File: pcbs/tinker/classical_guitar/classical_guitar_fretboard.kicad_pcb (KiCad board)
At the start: 2 copper layers, 192 parts, among them Q1 AO3401A, U1 AT42QT1110-A, U2 AT42QT1110-A, U3 AT42QT1110-A, U4 MP2359

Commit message: Layed out AT32QT1110
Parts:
- moved JPmiso3 419.5 mm to (77.8, 172.2)
- moved JPsck3 419.5 mm to (72.2, 172.2)
- moved Rs26 407.5 mm to (60.1, 173.8), turned to 90 degrees
- moved Cs25 405.5 mm to (55.4, 171.2), turned to 180 degrees
- moved Cs21 403.5 mm to (53.2, 157.5)
- moved Cd5 398.5 mm to (52.2, 164.0), turned to 270 degrees
- moved Cd6 398.4 mm to (59.9, 164.1), turned to 90 degrees
- moved Rs36 397.7 mm to (57.7, 156.6), turned to 90 degrees
- moved Cs23 397.7 mm to (50.8, 166.9), turned to 270 degrees
- moved Rs39 392.6 mm to (55.9, 156.6), turned to 270 degrees
- moved Cs26 388.6 mm to (59.1, 171.2), turned to 180 degrees
- moved Rs25 383.4 mm to (56.3, 173.8), turned to 90 degrees
- moved Rs28 381.5 mm to (67.6, 162.7)
- moved Cs30 380.6 mm to (60.5, 157.5)
- moved JPmosi3 376.1 mm to (64.4, 172.7), turned to 90 degrees
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- renumbered Cs11 to Cs1, Cs20 to Cs10, Cs21 to Cs11, Cs22 to Cs12, Cs23 to Cs13, Cs24 to Cs14, Cs25 to Cs15, Cs26 to Cs16, Cs27 to Cs17, Cs28 to Cs18, Cs29 to Cs19, Cs12 to Cs2, Cs30 to Cs20, Cs1 to Cs21, Cs2 to Cs22, Cs3 to Cs23, Cs4 to Cs24, Cs5 to Cs25, Cs6 to Cs26, Cs7 to Cs27, Cs8 to Cs28, Cs9 to Cs29, Cs13 to Cs3, Cs10 to Cs30, Cs14 to Cs4, Cs15 to Cs5, Cs16 to Cs6, Cs17 to Cs7, Cs18 to Cs8, Cs19 to Cs9
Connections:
- Cs1 pad 1: Net-(Cs11-Pad1) -> Net-(Cs1-Pad1)
- Cs10 pad 1: Net-(Cs20-Pad1) -> Net-(Cs10-Pad1)
- Cs11 pad 1: Net-(Cs21-Pad1) -> Net-(Cs11-Pad1)
- Cs12 pad 1: Net-(Cs22-Pad1) -> Net-(Cs12-Pad1)
- Cs13 pad 1: Net-(Cs23-Pad1) -> Net-(Cs13-Pad1)
- Cs14 pad 1: Net-(Cs24-Pad1) -> Net-(Cs14-Pad1)
- Cs15 pad 1: Net-(Cs25-Pad1) -> Net-(Cs15-Pad1)
- Cs16 pad 1: Net-(Cs26-Pad1) -> Net-(Cs16-Pad1)
- Cs17 pad 1: Net-(Cs27-Pad1) -> Net-(Cs17-Pad1)
- Cs18 pad 1: Net-(Cs28-Pad1) -> Net-(Cs18-Pad1)
- Cs19 pad 1: Net-(Cs29-Pad1) -> Net-(Cs19-Pad1)
- Cs2 pad 1: Net-(Cs12-Pad1) -> Net-(Cs2-Pad1)
- Cs20 pad 1: Net-(Cs30-Pad1) -> Net-(Cs20-Pad1)
- Cs21 pad 1: Net-(Cs1-Pad1) -> Net-(Cs21-Pad1)
- Cs22 pad 1: Net-(Cs2-Pad1) -> Net-(Cs22-Pad1)
- Cs23 pad 1: Net-(Cs3-Pad1) -> Net-(Cs23-Pad1)
- Cs24 pad 1: Net-(Cs4-Pad1) -> Net-(Cs24-Pad1)
- Cs25 pad 1: Net-(Cs5-Pad1) -> Net-(Cs25-Pad1)
- Cs26 pad 1: Net-(Cs6-Pad1) -> Net-(Cs26-Pad1)
- Cs27 pad 1: Net-(Cs7-Pad1) -> Net-(Cs27-Pad1)
- Cs28 pad 1: Net-(Cs8-Pad1) -> Net-(Cs28-Pad1)
- Cs29 pad 1: Net-(Cs9-Pad1) -> Net-(Cs29-Pad1)
- Cs3 pad 1: Net-(Cs13-Pad1) -> Net-(Cs3-Pad1)
- Cs30 pad 1: Net-(Cs10-Pad1) -> Net-(Cs30-Pad1)
- Cs4 pad 1: Net-(Cs14-Pad1) -> Net-(Cs4-Pad1)
- Cs5 pad 1: Net-(Cs15-Pad1) -> Net-(Cs5-Pad1)
- Cs6 pad 1: Net-(Cs16-Pad1) -> Net-(Cs6-Pad1)
- Cs7 pad 1: Net-(Cs17-Pad1) -> Net-(Cs7-Pad1)
- Cs8 pad 1: Net-(Cs18-Pad1) -> Net-(Cs8-Pad1)
- Cs9 pad 1: Net-(Cs19-Pad1) -> Net-(Cs9-Pad1)
- Rs1 pad 1: /Electrode21 -> /Electrode1
- Rs10 pad 1: /Electrode30 -> /Electrode10
- Rs11 pad 1: /Electrode1 -> /Electrode11
- Rs12 pad 1: /Electrode2 -> /Electrode12
- Rs13 pad 1: /Electrode3 -> /Electrode13
- Rs14 pad 1: /Electrode4 -> /Electrode14
- Rs15 pad 1: /Electrode5 -> /Electrode15
- Rs16 pad 1: /Electrode6 -> /Electrode16
- Rs17 pad 1: /Electrode7 -> /Electrode17
- Rs18 pad 1: /Electrode8 -> /Electrode18
- Rs19 pad 1: /Electrode9 -> /Electrode19
- Rs2 pad 1: /Electrode22 -> /Electrode2
- Rs20 pad 1: /Electrode10 -> /Electrode20
- Rs21 pad 1: /Electrode11 -> /Electrode21
- Rs22 pad 1: /Electrode12 -> /Electrode22
- Rs23 pad 1: /Electrode13 -> /Electrode23
- Rs24 pad 1: /Electrode14 -> /Electrode24
- Rs25 pad 1: /Electrode15 -> /Electrode25
- Rs26 pad 1: /Electrode16 -> /Electrode26
- Rs27 pad 1: /Electrode17 -> /Electrode27
- Rs28 pad 1: /Electrode18 -> /Electrode28
- Rs29 pad 1: /Electrode19 -> /Electrode29
- Rs3 pad 1: /Electrode23 -> /Electrode3
- Rs30 pad 1: /Electrode20 -> /Electrode30
- Rs4 pad 1: /Electrode24 -> /Electrode4
- Rs5 pad 1: /Electrode25 -> /Electrode5
- Rs6 pad 1: /Electrode26 -> /Electrode6
- Rs7 pad 1: /Electrode27 -> /Electrode7
- Rs8 pad 1: /Electrode28 -> /Electrode8
- Rs9 pad 1: /Electrode29 -> /Electrode9
- U1 pad 1: Net-(Cs11-Pad1) -> Net-(Cs1-Pad1)
- U1 pad 11: Net-(Cs15-Pad1) -> Net-(Cs5-Pad1)
- U1 pad 13: Net-(Cs16-Pad1) -> Net-(Cs6-Pad1)
- U1 pad 19: Net-(Cs17-Pad1) -> Net-(Cs7-Pad1)
- U1 pad 22: Net-(Cs18-Pad1) -> Net-(Cs8-Pad1)
- U1 pad 25: Net-(Cs19-Pad1) -> Net-(Cs9-Pad1)
- U1 pad 27: Net-(Cs20-Pad1) -> Net-(Cs10-Pad1)
- U1 pad 3: Net-(Cs12-Pad1) -> Net-(Cs2-Pad1)
- U1 pad 6: Net-(Cs13-Pad1) -> Net-(Cs3-Pad1)
- U1 pad 9: Net-(Cs14-Pad1) -> Net-(Cs4-Pad1)
- U2 pad 1: Net-(Cs21-Pad1) -> Net-(Cs11-Pad1)
- U2 pad 11: Net-(Cs25-Pad1) -> Net-(Cs15-Pad1)
- U2 pad 13: Net-(Cs26-Pad1) -> Net-(Cs16-Pad1)
- U2 pad 19: Net-(Cs27-Pad1) -> Net-(Cs17-Pad1)
- U2 pad 22: Net-(Cs28-Pad1) -> Net-(Cs18-Pad1)
- U2 pad 25: Net-(Cs29-Pad1) -> Net-(Cs19-Pad1)
- U2 pad 27: Net-(Cs30-Pad1) -> Net-(Cs20-Pad1)
- U2 pad 3: Net-(Cs22-Pad1) -> Net-(Cs12-Pad1)
- U2 pad 6: Net-(Cs23-Pad1) -> Net-(Cs13-Pad1)
- U2 pad 9: Net-(Cs24-Pad1) -> Net-(Cs14-Pad1)
- U3 pad 1: Net-(Cs1-Pad1) -> Net-(Cs21-Pad1)
- U3 pad 11: Net-(Cs5-Pad1) -> Net-(Cs25-Pad1)
- U3 pad 13: Net-(Cs6-Pad1) -> Net-(Cs26-Pad1)
- U3 pad 19: Net-(Cs7-Pad1) -> Net-(Cs27-Pad1)
- U3 pad 22: Net-(Cs8-Pad1) -> Net-(Cs28-Pad1)
- U3 pad 25: Net-(Cs9-Pad1) -> Net-(Cs29-Pad1)
- U3 pad 27: Net-(Cs10-Pad1) -> Net-(Cs30-Pad1)
- U3 pad 3: Net-(Cs2-Pad1) -> Net-(Cs22-Pad1)
- U3 pad 6: Net-(Cs3-Pad1) -> Net-(Cs23-Pad1)
- U3 pad 9: Net-(Cs4-Pad1) -> Net-(Cs24-Pad1)

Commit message: Replaced jumper pads
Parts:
- JPch1, JPch2, JPch3, JPe1, JPe10, JPe11, JPe12, JPe13, JPe14, JPe15, JPe16, JPe17, JPe18, JPe19, JPe2, JPe20, JPe21, JPe22, JPe23, JPe24, JPe25, JPe26, JPe27, JPe28, JPe29, JPe3, JPe30, JPe4, JPe5, JPe6, JPe7, JPe8, JPe9, JPmiso1, JPmiso2, JPmiso3, JPmosi1, JPmosi2, JPmosi3, JPsck1, JPsck2, JPsck3: value Jumper_3_B12 -> SolderJumper_3_Open; footprint Jumper:SolderJumper-3_P1.3mm_Bridged12_RoundedPad1.0x1.5mm_NumberLabels -> Jumper:SolderJumper-3_P1.3mm_Open_RoundedPad1.0x1.5mm_NumberLabels
- moved JPsck1 398.9 mm to (172.1, 131.6)
- moved JPmosi2 392.2 mm to (172.1, 128.1)
- moved JPe11 384.6 mm to (143.8, 131.6)
- moved JPe29 383.7 mm to (160.8, 131.6)
- moved JPe27 382.5 mm to (166.4, 124.5)
- moved JPmiso2 382.5 mm to (172.1, 124.5)
- moved JPmiso1 379.6 mm to (166.4, 128.1)
- moved JPe4 378.0 mm to (143.8, 124.5)
- moved JPe17 376.3 mm to (149.4, 131.6)
- moved JPe13 374.5 mm to (149.4, 128.1)
- moved JPe18 373.5 mm to (166.4, 117.4)
- moved JPch3 372.9 mm to (149.4, 113.9)
- moved JPe1 372.7 mm to (143.8, 121.0)
- moved JPsck2 372.5 mm to (177.7, 128.1)
- moved JPe8 371.5 mm to (160.8, 113.9)
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
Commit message: Trace for 5-to-32 decoder before replacement with 4-to-16 decoder
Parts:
- E1, E10, E11, E12, E13, E14, E15, E16, E17, E18, E19, E2, E20, E21, E22, E23, E24, E25, E26, E27, E28, E29, E3, E30, E4, E5, E6, E7, E8, E9: moved to B.Cu
- Jdecoder_output1: value Conn_02x16_Odd_Even -> Conn_01x32; footprint Connector_PinSocket_2.54mm:PinSocket_2x16_P2.54mm_Vertical -> Connector_PinSocket_2.54mm:PinSocket_1x32_P2.54mm_Vertical
- moved E30 280.6 mm to (170.0, 35.0)
- moved E21 278.2 mm to (170.0, 170.0)
- moved E29 268.4 mm to (170.0, 50.0)
- moved E22 265.9 mm to (170.0, 155.0)
- moved E28 258.7 mm to (170.0, 65.0)
- moved E20 258.5 mm to (155.0, 35.0)
- moved E23 258.0 mm to (170.0, 140.0)
- moved E11 257.8 mm to (155.0, 170.0)
- moved E27 252.5 mm to (170.0, 80.0)
- moved E24 251.0 mm to (170.0, 125.0)
- moved E25 248.9 mm to (170.0, 110.0)
- moved E26 248.6 mm to (170.0, 95.0)
- moved E19 245.9 mm to (155.0, 50.0)
- moved E12 244.3 mm to (155.0, 155.0)
- moved E10 239.6 mm to (140.0, 35.0)
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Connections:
- net /~OSS1 renamed /5_to_32_decoder/~Y0
- net /~OSS10 renamed /5_to_32_decoder/~Y9
- net /~OSS11 renamed /5_to_32_decoder/~Y10
- net /~OSS12 renamed /5_to_32_decoder/~Y11
- net /~OSS13 renamed /5_to_32_decoder/~Y12
- net /~OSS14 renamed /5_to_32_decoder/~Y13
- net /~OSS15 renamed /5_to_32_decoder/~Y14
- net /~OSS16 renamed /5_to_32_decoder/~Y15
- net /~OSS17 renamed /5_to_32_decoder/~Y16
- net /~OSS18 renamed /5_to_32_decoder/~Y17
- net /~OSS19 renamed /5_to_32_decoder/~Y18
- net /~OSS2 renamed /5_to_32_decoder/~Y1
- net /~OSS20 renamed /5_to_32_decoder/~Y19
- net /~OSS21 renamed /5_to_32_decoder/~Y20
- net /~OSS22 renamed /5_to_32_decoder/~Y21
- net /~OSS23 renamed /5_to_32_decoder/~Y22
- net /~OSS24 renamed /5_to_32_decoder/~Y23
- net /~OSS25 renamed /5_to_32_decoder/~Y24
- net /~OSS26 renamed /5_to_32_decoder/~Y25
- net /~OSS27 renamed /5_to_32_decoder/~Y26
- net /~OSS28 renamed /5_to_32_decoder/~Y27
- net /~OSS29 renamed /5_to_32_decoder/~Y28
- net /~OSS3 renamed /5_to_32_decoder/~Y2
- net /~OSS30 renamed /5_to_32_decoder/~Y29
- net /~OSS31 renamed /5_to_32_decoder/~Y30
- net /~OSS32 renamed /5_to_32_decoder/~Y31
- net /~OSS4 renamed /5_to_32_decoder/~Y3
- net /~OSS5 renamed /5_to_32_decoder/~Y4
- net /~OSS6 renamed /5_to_32_decoder/~Y5
- net /~OSS7 renamed /5_to_32_decoder/~Y6
- net /~OSS8 renamed /5_to_32_decoder/~Y7
- net /~OSS9 renamed /5_to_32_decoder/~Y8
- JPe1 pad 1: /Electrode1 -> Net-(E1-Pad1)
- JPe1 pad 2: Net-(E1-Pad1) -> /Electrode1
- JPe10 pad 1: /Electrode10 -> Net-(E10-Pad1)
- JPe10 pad 2: Net-(E10-Pad1) -> /Electrode10
- JPe11 pad 1: /Electrode11 -> Net-(E11-Pad1)
- JPe11 pad 2: Net-(E11-Pad1) -> /Electrode11
- JPe12 pad 1: /Electrode12 -> Net-(E12-Pad1)
- JPe12 pad 2: Net-(E12-Pad1) -> /Electrode12
- JPe13 pad 1: /Electrode13 -> Net-(E13-Pad1)
- JPe13 pad 2: Net-(E13-Pad1) -> /Electrode13
- JPe14 pad 1: /Electrode14 -> Net-(E14-Pad1)
- JPe14 pad 2: Net-(E14-Pad1) -> /Electrode14
- JPe15 pad 1: /Electrode15 -> Net-(E15-Pad1)
- JPe15 pad 2: Net-(E15-Pad1) -> /Electrode15
- JPe16 pad 1: /Electrode16 -> Net-(E16-Pad1)
- JPe16 pad 2: Net-(E16-Pad1) -> /Electrode16
- JPe17 pad 1: /Electrode17 -> Net-(E17-Pad1)
- JPe17 pad 2: Net-(E17-Pad1) -> /Electrode17
- JPe18 pad 1: /Electrode18 -> Net-(E18-Pad1)
- JPe18 pad 2: Net-(E18-Pad1) -> /Electrode18
- JPe19 pad 1: /Electrode19 -> Net-(E19-Pad1)
- JPe19 pad 2: Net-(E19-Pad1) -> /Electrode19
- JPe2 pad 1: /Electrode2 -> Net-(E2-Pad1)
- JPe2 pad 2: Net-(E2-Pad1) -> /Electrode2
- JPe20 pad 1: /Electrode20 -> Net-(E20-Pad1)
- JPe20 pad 2: Net-(E20-Pad1) -> /Electrode20
- JPe21 pad 1: /Electrode21 -> Net-(E21-Pad1)
- JPe21 pad 2: Net-(E21-Pad1) -> /Electrode21
- JPe22 pad 1: /Electrode22 -> Net-(E22-Pad1)
- JPe22 pad 2: Net-(E22-Pad1) -> /Electrode22
- JPe23 pad 1: /Electrode23 -> Net-(E23-Pad1)
- JPe23 pad 2: Net-(E23-Pad1) -> /Electrode23
- JPe24 pad 1: /Electrode24 -> Net-(E24-Pad1)
- JPe24 pad 2: Net-(E24-Pad1) -> /Electrode24
- JPe25 pad 1: /Electrode25 -> Net-(E25-Pad1)
- JPe25 pad 2: Net-(E25-Pad1) -> /Electrode25
- JPe26 pad 1: /Electrode26 -> Net-(E26-Pad1)
- JPe26 pad 2: Net-(E26-Pad1) -> /Electrode26
- JPe27 pad 1: /Electrode27 -> Net-(E27-Pad1)
- JPe27 pad 2: Net-(E27-Pad1) -> /Electrode27
- JPe28 pad 1: /Electrode28 -> Net-(E28-Pad1)
- JPe28 pad 2: Net-(E28-Pad1) -> /Electrode28
- JPe29 pad 1: /Electrode29 -> Net-(E29-Pad1)
- JPe29 pad 2: Net-(E29-Pad1) -> /Electrode29
- JPe3 pad 1: /Electrode3 -> Net-(E3-Pad1)
- JPe3 pad 2: Net-(E3-Pad1) -> /Electrode3
- JPe30 pad 1: /Electrode30 -> Net-(E30-Pad1)
- JPe30 pad 2: Net-(E30-Pad1) -> /Electrode30
- JPe4 pad 1: /Electrode4 -> Net-(E4-Pad1)
- JPe4 pad 2: Net-(E4-Pad1) -> /Electrode4
- JPe5 pad 1: /Electrode5 -> Net-(E5-Pad1)
- JPe5 pad 2: Net-(E5-Pad1) -> /Electrode5
- JPe6 pad 1: /Electrode6 -> Net-(E6-Pad1)
- JPe6 pad 2: Net-(E6-Pad1) -> /Electrode6
- JPe7 pad 1: /Electrode7 -> Net-(E7-Pad1)
- JPe7 pad 2: Net-(E7-Pad1) -> /Electrode7
- JPe8 pad 1: /Electrode8 -> Net-(E8-Pad1)
- JPe8 pad 2: Net-(E8-Pad1) -> /Electrode8
- JPe9 pad 1: /Electrode9 -> Net-(E9-Pad1)
- JPe9 pad 2: Net-(E9-Pad1) -> /Electrode9
- JPmiso1 pad 1: /MISO1 -> /C_MISO
- JPmiso1 pad 2: /C_MISO -> /MISO1
- JPmiso2 pad 1: /MISO2 -> /C_MISO
- JPmiso2 pad 2: /C_MISO -> /MISO2
- JPmiso3 pad 1: /MISO3 -> /C_MISO
- JPmiso3 pad 2: /C_MISO -> /MISO3
- JPmosi1 pad 1: /MOSI1 -> /C_MOSI
- JPmosi1 pad 2: /C_MOSI -> /MOSI1
- JPmosi2 pad 1: /MOSI2 -> /C_MOSI
- JPmosi2 pad 2: /C_MOSI -> /MOSI2
- JPmosi3 pad 1: /MOSI3 -> /C_MOSI
- JPmosi3 pad 2: /C_MOSI -> /MOSI3
- JPsck1 pad 1: /SCK1 -> /C_SCK
- JPsck1 pad 2: /C_SCK -> /SCK1
- JPsck2 pad 1: /SCK2 -> /C_SCK
- JPsck2 pad 2: /C_SCK -> /SCK2
- JPsck3 pad 1: /SCK3 -> /C_SCK
- JPsck3 pad 2: /C_SCK -> /SCK3
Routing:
- net /5_to_32_decoder/~Y31: track 0.00 -> 50.7 mm
- net /5_to_32_decoder/~Y0: track 0.00 -> 40.7 mm
- net /5_to_32_decoder/~Y30: track 0.00 -> 39.4 mm
- net /5_to_32_decoder/~Y1: track 0.00 -> 38.7 mm
- net /5_to_32_decoder/~Y29: track 0.00 -> 37.8 mm
- net /5_to_32_decoder/~Y7: track 0.00 -> 36.9 mm
- net /5_to_32_decoder/~Y2: track 0.00 -> 36.5 mm
- net /5_to_32_decoder/~Y23: track 0.00 -> 36.3 mm
- net /5_to_32_decoder/~Y28: track 0.00 -> 36.0 mm
- net /5_to_32_decoder/~Y3: track 0.00 -> 35.0 mm
- net /5_to_32_decoder/~Y27: track 0.00 -> 34.3 mm
- net /5_to_32_decoder/~Y4: track 0.00 -> 32.7 mm
- net /5_to_32_decoder/~Y26: track 0.00 -> 31.9 mm
- net /5_to_32_decoder/~Y5: track 0.00 -> 30.6 mm
- net /5_to_32_decoder/~Y25: track 0.00 -> 29.7 mm
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
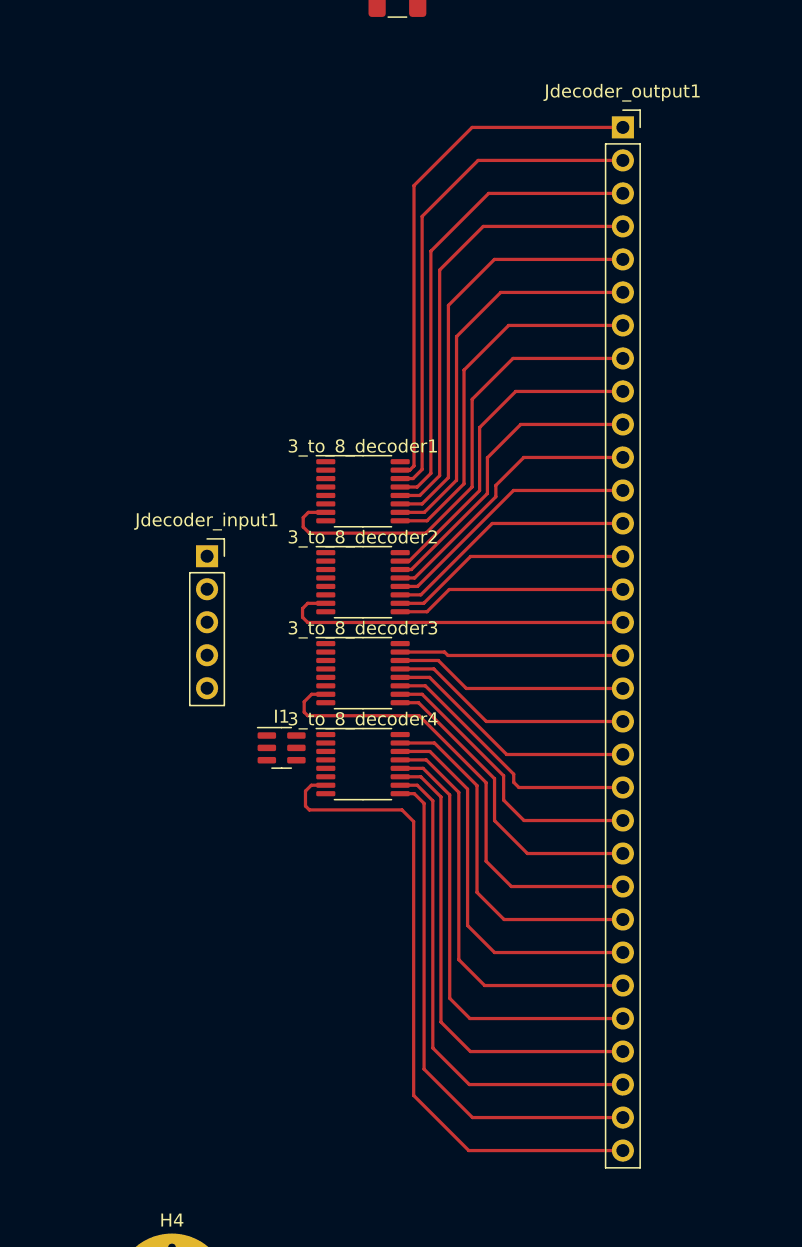
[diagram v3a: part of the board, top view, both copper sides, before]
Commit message: Replaced 5-to-32 decoder with 4-to-16 decoder
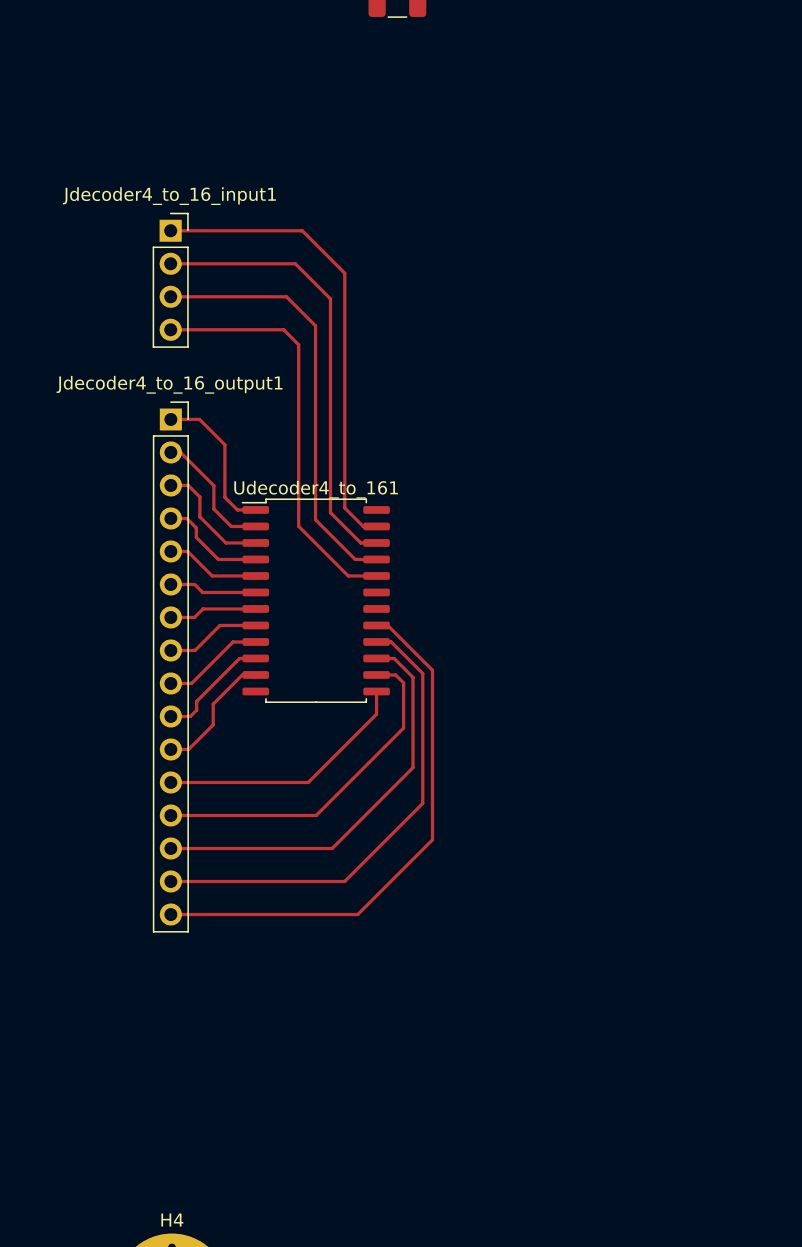
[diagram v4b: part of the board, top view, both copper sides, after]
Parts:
- removed 3_to_8_decoder1, 3_to_8_decoder2, 3_to_8_decoder3, 3_to_8_decoder4: 74HC138, Package_SO:TSSOP-16_4.4x5mm_P0.65mm
- removed I1: MC74HC1G04, Package_SO:SC-74-6_1.5x2.9mm_P0.95mm
- removed Jdecoder_input1: Conn_01x05_Male, Connector_PinSocket_2.54mm:PinSocket_1x05_P2.54mm_Vertical
- removed Jdecoder_output1: Conn_01x32, Connector_PinSocket_2.54mm:PinSocket_1x32_P2.54mm_Vertical
- added Jdecoder4_to_16_input1: Conn_01x04_Male, Connector_PinSocket_2.54mm:PinSocket_1x04_P2.54mm_Vertical, F.Cu at (31.1, 70.5)
- added Jdecoder4_to_16_output1: Conn_01x16, Connector_PinSocket_2.54mm:PinSocket_1x16_P2.54mm_Vertical, F.Cu at (31.2, 85.0)
- added Udecoder4_to_161: CD74HC154ME4, Package_SO:SOIC-24W_7.5x15.4mm_P1.27mm, F.Cu at (42.3, 99.0)
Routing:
- net /5_to_32_decoder/~Y31: track 50.7 -> 0.00 mm
- net Net-(Jdecoder4_to_16_output1-Pad16): track 0.00 -> 41.3 mm
- net /5_to_32_decoder/~Y0: track 40.7 -> 0.00 mm
- net /5_to_32_decoder/~Y30: track 39.4 -> 0.00 mm
- net /5_to_32_decoder/~Y1: track 38.7 -> 0.00 mm
- net /5_to_32_decoder/~Y29: track 37.8 -> 0.00 mm
- net /5_to_32_decoder/~Y7: track 36.9 -> 0.00 mm
- net /5_to_32_decoder/~Y2: track 36.5 -> 0.00 mm
- net Net-(Jdecoder4_to_16_output1-Pad15): track 0.00 -> 36.4 mm
- net /5_to_32_decoder/~Y23: track 36.3 -> 0.00 mm
- net /5_to_32_decoder/~Y28: track 36.0 -> 0.00 mm
- net Net-(Jdecoder4_to_16_input1-Pad1): track 0.00 -> 35.9 mm
- net /5_to_32_decoder/~Y3: track 35.0 -> 0.00 mm
- net Net-(Jdecoder4_to_16_input1-Pad2): track 0.00 -> 34.4 mm
- net /5_to_32_decoder/~Y27: track 34.3 -> 0.00 mm
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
